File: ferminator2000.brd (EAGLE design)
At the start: 111.1 x 58.3 mm, 125 parts, among them CN1 MINIB, IC1 FT232RL, IC2 REF01D, Q1 STP5NA50, Q2 STP5NA50, SW1 ENCODER_SW1-PEC12, U1 DSPIC33FJ256GP510A, U2 AD8495

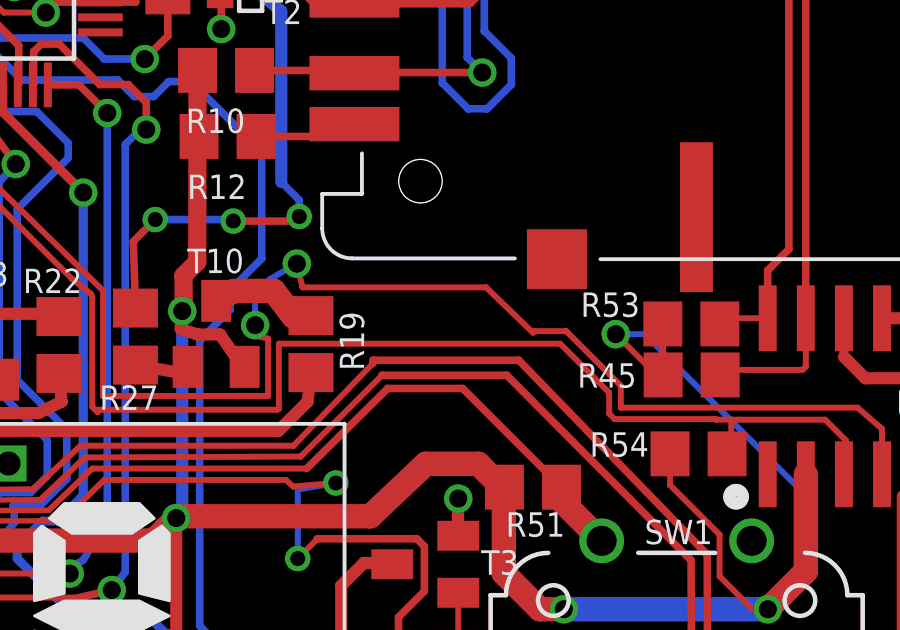
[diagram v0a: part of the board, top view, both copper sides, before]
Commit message: Added 0.1uF decoupling cap to RTC
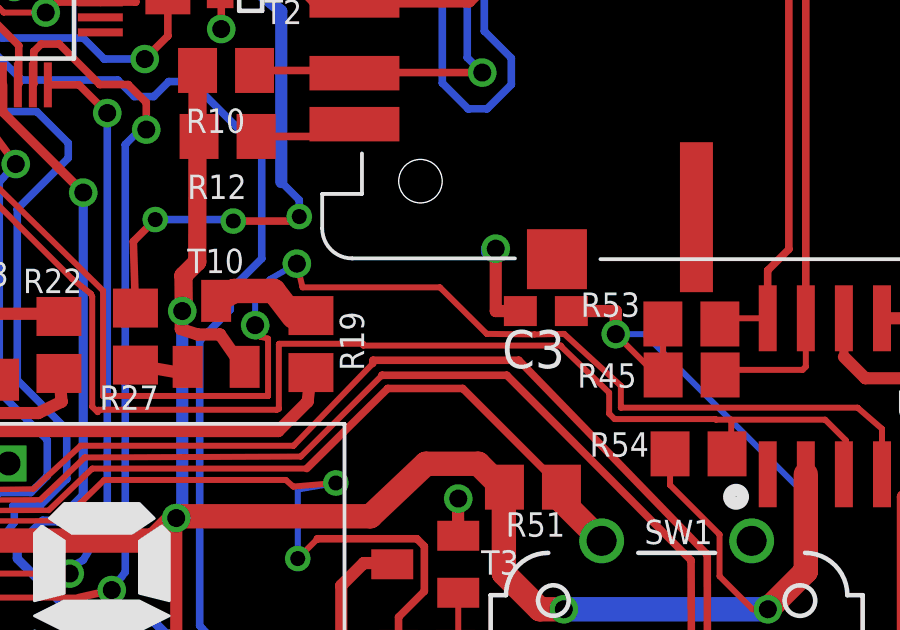
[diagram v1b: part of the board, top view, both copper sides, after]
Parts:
- added C3: .1u, rcl:C0603
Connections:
- net GND: now also C3.2
- net VDD: now also C3.1
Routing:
- net GND: track 231.2 -> 234.5 mm, vias 41 -> 42
- net VDD: track 424.2 -> 426.4 mm
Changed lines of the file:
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@@
 <layer number="19" name="Unrouted" color="6" fill="1" visible="yes" active="yes"/>
 <layer number="20" name="Dimension" color="15" fill="1" visible="yes" active="yes"/>
-<layer number="21" name="tPlace" color="7" fill="1" visible="no" active="yes"/>
-<layer number="22" name="bPlace" color="7" fill="1" visible="no" active="yes"/>
-<layer number="23" name="tOrigins" color="15" fill="1" visible="no" active="yes"/>
-<layer number="24" name="bOrigins" color="15" fill="1" visible="no" active="yes"/>
+<layer number="21" name="tPlace" color="7" fill="1" visible="yes" active="yes"/>
+<layer number="22" name="bPlace" color="7" fill="1" visible="yes" active="yes"/>
+<layer number="23" name="tOrigins" color="15" fill="1" visible="yes" active="yes"/>
+<layer number="24" name="bOrigins" color="15" fill="1" visible="yes" active="yes"/>
 <layer number="25" name="tNames" color="7" fill="1" visible="yes" active="yes"/>
 <layer number="26" name="bNames" color="7" fill="1" visible="yes" active="yes"/>
@@
 <attribute name="VALUE" x="94.925" y="23.32" size="1.27" layer="27" rot="R180"/>
 </element>
+<element name="C3" library="rcl" package="C0603" value=".1u" x="89.2" y="25.54" rot="R180"/>
 </elements>
 <signals>
@@
 <wire x1="97.865" y1="19.4" x2="97.865" y2="16.865" width="0.2" layer="16"/>
 <wire x1="97.865" y1="16.865" x2="96.6" y2="15.6" width="0.2" layer="16"/>
+<contactref element="C3" pad="1"/>
+<wire x1="90.05" y1="25.54" x2="91.53" y2="25.54" width="0.4064" layer="1"/>
+<wire x1="91.53" y1="25.54" x2="91.53" y2="24.77" width="0.4064" layer="1"/>
 </signal>
 <signal name="GND">
@@
 <wire x1="101.8" y1="25.2" x2="101.8" y2="25.15" width="0.4064" layer="16"/>
 <wire x1="101.8" y1="25.15" x2="101.95" y2="25" width="0.4064" layer="16"/>
+<contactref element="C3" pad="2"/>
+<wire x1="88.35" y1="25.54" x2="87.53" y2="25.54" width="0.4064" layer="1"/>
+<wire x1="87.53" y1="25.54" x2="87.53" y2="27.62" width="0.4064" layer="1"/>
+<via x="87.53" y="27.62" extent="1-16" drill="0.6"/>
+<wire x1="87.53" y1="27.62" x2="87.24" y2="27.62" width="0.4064" layer="16"/>
+<wire x1="87.24" y1="27.62" x2="87.24" y2="27.51" width="0.4064" layer="16"/>
 </signal>
 <signal name="PGD1">
@@
 <wire x1="80.3" y1="22.28" x2="80.3" y2="24.43" width="0.2" layer="1"/>
 <wire x1="80.3" y1="24.43" x2="80.31" y2="24.45" width="0.2" layer="1"/>
-<wire x1="80.31" y1="24.45" x2="89.68" y2="24.45" width="0.2" layer="1"/>
+<wire x1="80.31" y1="24.45" x2="83.11" y2="24.45" width="0.2" layer="1"/>
+<wire x1="83.11" y1="24.45" x2="83.11" y2="24.39" width="0.2" layer="1"/>
+<wire x1="83.11" y1="24.39" x2="89.7" y2="24.39" width="0.2" layer="1"/>
+<wire x1="89.7" y1="24.39" x2="89.73" y2="24.34" width="0.2" layer="1"/>
 <wire x1="94.87" y1="21.92" x2="95.38" y2="21.92" width="0.2" layer="1"/>
 <wire x1="95.38" y1="21.92" x2="98.51" y2="21.92" width="0.2" layer="1"/>
@@
 <wire x1="95.24" y1="20.78" x2="95.38" y2="20.92" width="0.2" layer="1"/>
 <wire x1="95.38" y1="20.92" x2="95.38" y2="21.92" width="0.2" layer="1"/>
-<wire x1="89.68" y1="24.45" x2="91.31" y2="22.82" width="0.2" layer="1"/>
+<wire x1="89.73" y1="24.34" x2="91.31" y2="22.82" width="0.2" layer="1"/>
 <wire x1="91.31" y1="22.82" x2="91.31" y2="22.12" width="0.2" layer="1"/>
 <wire x1="91.31" y1="22.12" x2="91.49" y2="21.94" width="0.2" layer="1"/>
@@
 <via x="80.9" y="27.12" extent="1-16" drill="0.6"/>
 <wire x1="80.9" y1="27.12" x2="81.09" y2="26.33" width="0.2" layer="1"/>
-<wire x1="81.09" y1="26.33" x2="87.21" y2="26.33" width="0.2" layer="1"/>
-<wire x1="87.21" y1="26.33" x2="88.77" y2="24.82" width="0.2" layer="1"/>
-<wire x1="88.77" y1="24.82" x2="88.82" y2="24.87" width="0.2" layer="1"/>
+<wire x1="81.09" y1="26.33" x2="85.67" y2="26.33" width="0.2" layer="1"/>
+<wire x1="85.67" y1="26.33" x2="87.23" y2="24.78" width="0.2" layer="1"/>
+<wire x1="87.23" y1="24.78" x2="88.82" y2="24.76" width="0.2" layer="1"/>
 <wire x1="91.7" y1="22.32" x2="99.59" y2="22.32" width="0.2" layer="1"/>
 <wire x1="99.59" y1="22.32" x2="100.405" y2="21.615" width="0.2" layer="1"/>
 <wire x1="100.405" y1="21.615" x2="100.405" y2="20.1" width="0.2" layer="1"/>
 <wire x1="91.7" y1="22.32" x2="91.7" y2="23.05" width="0.2" layer="1"/>
-<wire x1="91.7" y1="23.05" x2="89.88" y2="24.87" width="0.2" layer="1"/>
-<wire x1="89.88" y1="24.87" x2="88.82" y2="24.87" width="0.2" layer="1"/>
+<wire x1="91.7" y1="23.05" x2="89.81" y2="24.78" width="0.2" layer="1"/>
+<wire x1="89.81" y1="24.78" x2="88.82" y2="24.76" width="0.2" layer="1"/>
 </signal>
 </signals>

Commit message: Tied REF pin of AD8495 (thermocouple driver) to ground
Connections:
- net GND: now also U2.2
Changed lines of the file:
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@@
 <wire x1="87.53" y1="27.62" x2="87.24" y2="27.62" width="0.4064" layer="16"/>
 <wire x1="87.24" y1="27.62" x2="87.24" y2="27.51" width="0.4064" layer="16"/>
+<contactref element="U2" pad="2"/>
+<wire x1="20.485" y1="26.82" x2="19.835" y2="26.82" width="0" layer="19" extent="1-1"/>
 </signal>
 <signal name="PGD1">
